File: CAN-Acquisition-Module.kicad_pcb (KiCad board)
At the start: 2 copper layers, 92 x 71 mm, 201 parts, among them J1 Conn_01x04, J10 OSTVN04A150, J11 OSTVN04A150, J12 OSTVN04A150, J13 OSTVN04A150, J2 Conn_01x02, J3 Conn_01x03, J4 Conn_02x05_Odd_Even, J5 OSTVN04A150, J6 OSTVN04A150, J7 USB_B_Micro, J8 OSTVN04A150, J9 OSTVN04A150, Q1 SI2318A, U1 TL431DBZ, U10 BD12734FVJ-E2, U2 S-8581AA, U3 M483SGCAE, U4 SN65HVD234, U5 BD12734FVJ-E2, U6 SCD30, U7 SHT35-DIS, U8 OPA4317IPWR, U9 ERC13232FN-1, Y1 12 MHz

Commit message: Added board settings
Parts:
- moved D2 19.8 mm to (37.8, 26.5)
- moved D6 1.42 mm to (100.4, 63.7), turned to 180 degrees
- moved D1 0.40 mm to (36.7, 23.0)
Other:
- copper layers 2 -> 4
- rule pad_to_mask_clearance: 0 -> 0.05

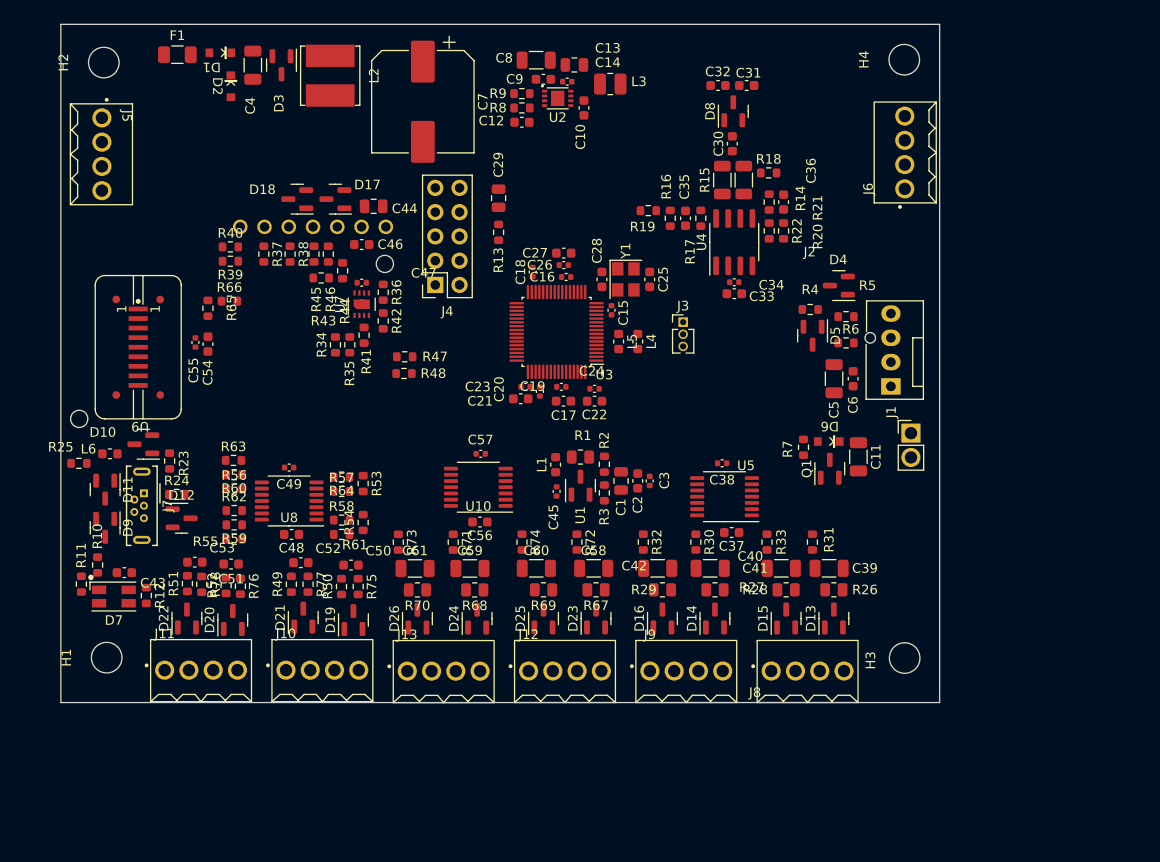
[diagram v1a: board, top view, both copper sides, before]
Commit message: Layout of analog section started
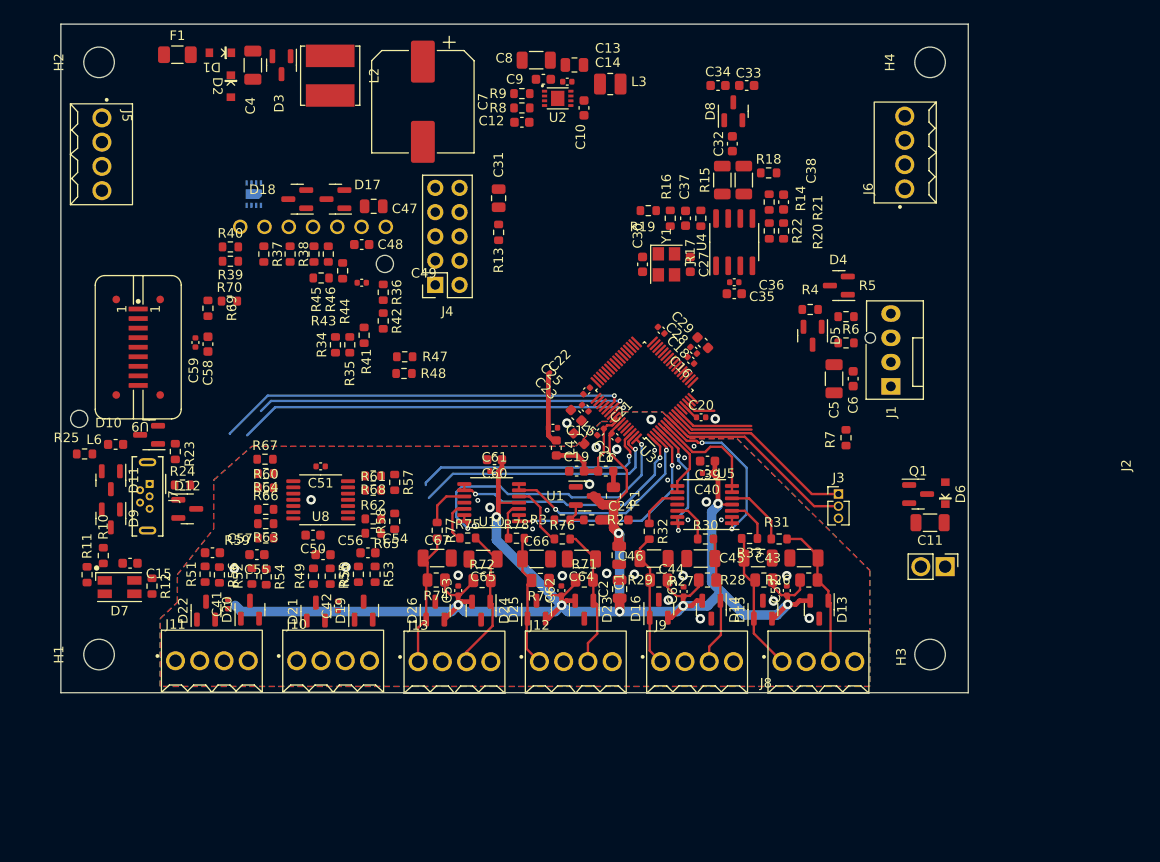
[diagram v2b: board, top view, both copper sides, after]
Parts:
- removed C3: 100 nF, Capacitor_SMD:C_0402_1005Metric
- added C41: 100 nF, Capacitor_SMD:C_0402_1005Metric, F.Cu at (37.5, 80.7)
- added C42: 100 nF, Capacitor_SMD:C_0402_1005Metric, F.Cu at (49.0, 80.9)
- added C52: 100 nF, Capacitor_SMD:C_0402_1005Metric, F.Cu at (96.0, 79.3)
- added C53: 100 nF, Capacitor_SMD:C_0402_1005Metric, F.Cu at (61.6, 79.3)
- added C62: 100 nF, Capacitor_SMD:C_0402_1005Metric, F.Cu at (72.4, 79.3)
- added C63: 100 nF, Capacitor_SMD:C_0402_1005Metric, F.Cu at (85.2, 79.4)
- C2: value 1 uF -> 10 uF; footprint Capacitor_SMD:C_0603_1608Metric -> Capacitor_SMD:C_0805_2012Metric
- U7: moved to B.Cu
- moved J3 24.3 mm to (101.4, 69.2)
- moved C20 23.3 mm to (87.0, 61.2), turned to 0 degrees
- moved C29 17.3 mm to (87.2, 53.4), turned to -45 degrees
- moved C28 16.3 mm to (86.2, 54.1), turned to -45 degrees
- moved U7 16.1 mm to (40.2, 37.8)
- moved J2 14.4 mm to (112.6, 76.8), turned to -90 degrees
- moved L4 14.0 mm to (71.9, 64.4)
- moved D6 13.3 mm to (112.6, 69.1), turned to 90 degrees
- moved C24 12.7 mm to (78.6, 71.9), turned to 0 degrees
- moved C2 11.5 mm to (78.5, 79.2), turned to 90 degrees
- moved C18 11.4 mm to (82.8, 52.0), turned to 135 degrees
- moved U3 11.1 mm to (81.1, 58.4), turned to 135 degrees
- moved L5 11.0 mm to (74.2, 63.4), turned to -45 degrees
- moved C11 10.2 mm to (111.0, 72.2), turned to 180 degrees
- moved C16 9.82 mm to (86.0, 55.2), turned to -45 degrees
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- renumbered C43 to C15, C15 to C16, C45 to C17, C16 to C18, C17 to C19, C18 to C20, C19 to C21, C20 to C22, C21 to C23, C22 to C24, C23 to C25, C24 to C26, C25 to C27, C26 to C28, C27 to C29, C28 to C30, C29 to C31, C30 to C32, C31 to C33, C32 to C34, C33 to C35, C34 to C36, C35 to C37, C36 to C38, C37 to C39, C38 to C40, C39 to C43, C40 to C44, C41 to C45, C42 to C46, C44 to C47, C46 to C48, C47 to C49, C48 to C50, C49 to C51, C50 to C54, C51 to C55, C52 to C56, C53 to C57, C54 to C58, C55 to C59, C56 to C60, C57 to C61, C58 to C64, C59 to C65, C60 to C66, C61 to C67, R75 to R53, R76 to R54, R77 to R55, R78 to R56, R53 to R57, R54 to R58, R55 to R59, R56 to R60, R57 to R61, R58 to R62, R59 to R63, R60 to R64, R61 to R65, R62 to R66, R63 to R67, R64 to R68, R65 to R69, R66 to R70, R67 to R71, R68 to R72, R69 to R73, R70 to R74, R71 to R75, R72 to R76, R73 to R77, R74 to R78
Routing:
- net +1V8: track 0.00 -> 168.5 mm, vias 0 -> 8
- net Net-(R10-Pad1): track 0.00 -> 43.7 mm, vias 0 -> 1
- net Net-(R12-Pad1): track 0.00 -> 42.1 mm, vias 0 -> 1
- net Net-(R11-Pad1): track 0.00 -> 39.6 mm, vias 0 -> 1
- net /ADC7: track 0.00 -> 30.9 mm, vias 0 -> 2
- net /ADC6: track 0.00 -> 27.0 mm, vias 0 -> 2
- net /ADC8: track 0.00 -> 26.9 mm, vias 0 -> 1
- net /ADC9: track 0.00 -> 26.0 mm, vias 0 -> 1
- net /ADC4: track 0.00 -> 24.6 mm, vias 0 -> 2
- net /ADC5: track 0.00 -> 22.9 mm, vias 0 -> 2
- net Net-(J3-Pad2): track 0.00 -> 21.2 mm
- net Net-(J3-Pad1): track 0.00 -> 20.5 mm
- net /ADC0: track 0.00 -> 18.5 mm, vias 0 -> 2
- net Net-(C43-Pad1): track 0.00 -> 15.6 mm
- net Net-(C45-Pad1): track 0.00 -> 15.4 mm
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- added copper zone on B.Cu, net GNDA
- added copper zone on F.Cu, net GNDA
- added copper zone on In1.Cu, net GNDA
- added copper zone on In2.Cu, net GNDA
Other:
- board size 92 x 71 mm -> 95 x 70 mm

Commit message: Analog section, screen and USB finished
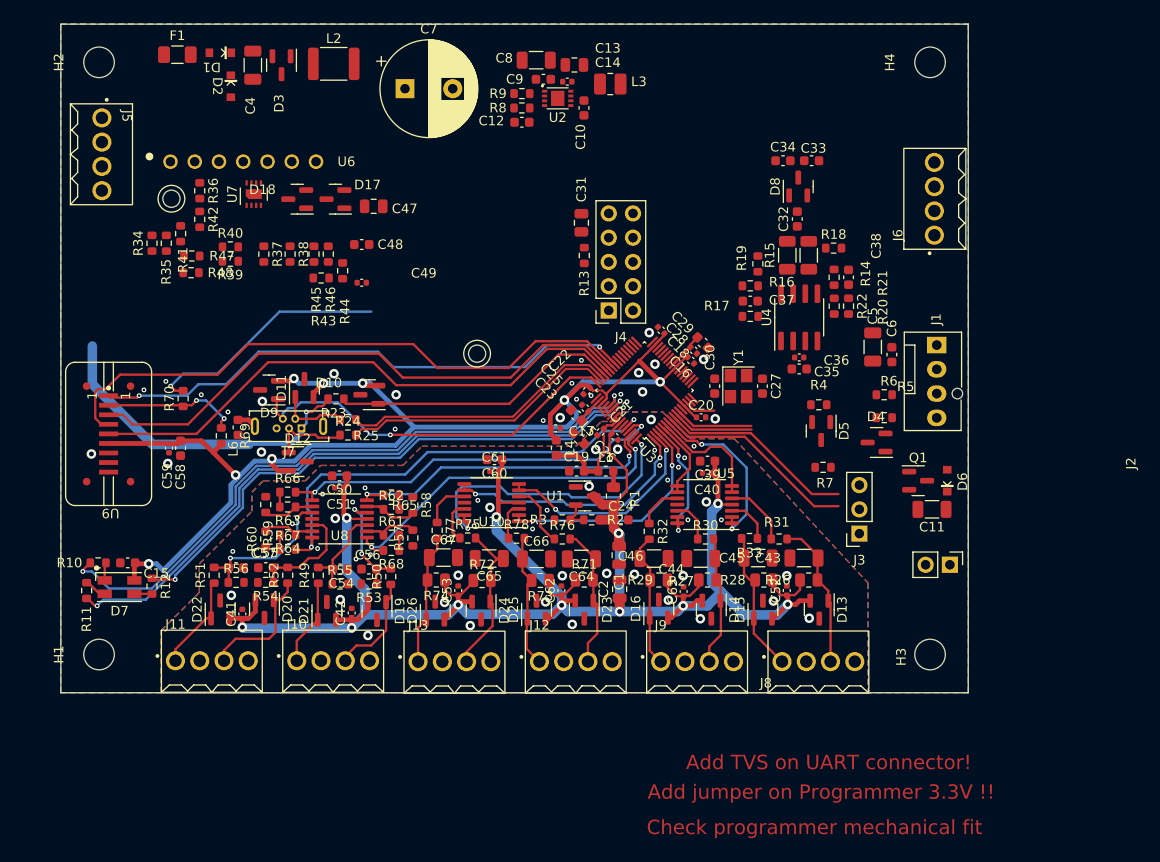
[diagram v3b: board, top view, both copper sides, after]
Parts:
- C7: footprint Capacitor_SMD:CP_Elec_10x10.5 -> Capacitor_THT:CP_Radial_D10.0mm_P5.00mm
- J3: footprint Connector_PinHeader_1.27mm:PinHeader_1x03_P1.27mm_Vertical -> Connector_PinSocket_2.54mm:PinSocket_1x03_P2.54mm_Vertical
- L2: value 330 uF -> 470 uF; footprint Inductor_SMD:L_Bourns_SRN6045TA -> CAN-Acquisition-Module:Murata_LQH43_1812(4532_Metric)
- U6, U7: moved to F.Cu
- moved R25 27.8 mm to (50.1, 61.4), turned to 0 degrees
- moved R47 24.7 mm to (33.7, 44.3)
- moved R48 24.7 mm to (33.6, 46.0)
- moved U6 23.6 mm to (31.5, 34.4), turned to 0 degrees
- moved D10 23.4 mm to (52.3, 58.8)
- moved D11 22.4 mm to (45.5, 58.1), turned to 90 degrees
- moved R34 22.0 mm to (29.5, 42.9)
- moved R35 22.0 mm to (31.0, 42.9)
- moved R36 22.0 mm to (34.5, 37.4)
- moved R41 22.0 mm to (32.5, 41.9)
- moved R42 22.0 mm to (34.5, 40.4)
- moved D9 21.3 mm to (41.8, 58.3), turned to 180 degrees
- moved J4 18.4 mm to (77.4, 50.0)
- moved R24 18.1 mm to (50.0, 63.0)
- moved R23 17.7 mm to (48.8, 59.2), turned to 0 degrees
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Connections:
- C56 pad 1: Net-(C56-Pad1) -> Net-(U8-Pad3)
- J4 pad 1: unconnected-(J4-Pad1) -> +3V3
- J4 pad 10: GND -> /MCU/UART0_RX
- J4 pad 2: +3V3 -> unconnected-(J4-Pad2)
- J4 pad 3: unconnected-(J4-Pad3) -> /MCU/ICE_DAT
- J4 pad 4: /MCU/ICE_DAT -> unconnected-(J4-Pad4)
- J4 pad 5: unconnected-(J4-Pad5) -> /MCU/ICE_CLK
- J4 pad 6: /MCU/ICE_CLK -> unconnected-(J4-Pad6)
- J4 pad 7: /MCU/UART0_TX -> /MCU/nRESET
- J4 pad 8: /MCU/nRESET -> /MCU/UART0_TX
- J4 pad 9: /MCU/UART0_RX -> GND
- R49 pad 2: Net-(C56-Pad1) -> Net-(U8-Pad3)
- R55 pad 1: Net-(C56-Pad1) -> Net-(U8-Pad3)
- U3 pad 8: Net-(J3-Pad2) -> Net-(J3-Pad1)
- U3 pad 9: Net-(J3-Pad1) -> Net-(J3-Pad2)
- U8 pad 1: /ADC9 -> /ADC8
- U8 pad 10: Net-(C55-Pad1) -> Net-(C57-Pad1)
- U8 pad 12: Net-(C57-Pad1) -> Net-(C55-Pad1)
- U8 pad 13: Net-(R59-Pad2) -> Net-(R60-Pad2)
- U8 pad 14: /ADC10 -> /ADC11
- U8 pad 2: Net-(R58-Pad2) -> Net-(R57-Pad2)
- U8 pad 3: Net-(C54-Pad1) -> Net-(U8-Pad3)
- U8 pad 5: Net-(C56-Pad1) -> Net-(C54-Pad1)
- U8 pad 6: Net-(R57-Pad2) -> Net-(R58-Pad2)
- U8 pad 7: /ADC8 -> /ADC9
- U8 pad 8: /ADC11 -> /ADC10
- U8 pad 9: Net-(R60-Pad2) -> Net-(R59-Pad2)
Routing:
- net +3V3: track 9.42 -> 141.2 mm, vias 0 -> 8
- net /MCU/SCREEN_CLK: track 0.00 -> 63.9 mm
- net /MCU/SCREEN_COMMAND/DATA: track 0.00 -> 59.4 mm
- net /MCU/SCREEN_MOSI: track 0.00 -> 58.8 mm
- net /MCU/SCREEN_SS: track 0.00 -> 57.6 mm, vias 0 -> 2
- net /ADC11: track 0.00 -> 47.8 mm, vias 0 -> 2
- net /ADC10: track 0.00 -> 42.4 mm, vias 0 -> 2
- net /MCU/USB_OTG_ID: track 0.00 -> 40.2 mm, vias 0 -> 1
- net /Power/V_USB: track 0.00 -> 34.3 mm, vias 0 -> 1
- net /MCU/USB_VBUS: track 0.00 -> 30.6 mm
- net /MCU/USB_D-: track 0.00 -> 29.1 mm
- net /MCU/USB_D+: track 0.00 -> 28.8 mm
- net +1V8: track 168.5 -> 197.0 mm, vias 8 -> 11
- net Net-(R11-Pad1): track 39.6 -> 67.8 mm, vias 1 -> 2
- net /MCU/PERIPHERAL_RESET: track 0.00 -> 25.7 mm, vias 0 -> 1
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- added copper zone on B.Cu, net GND
- added copper zone on F.Cu, net GND
- added copper zone on In1.Cu, net GND
- added copper zone on In2.Cu, net GND
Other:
- board text added: "Add TVS on UART connector!"
- board text added: "Add jumper on Programmer 3.3V !!"
- board text added: "Check programmer mechanical fit"

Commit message: Finished power outputs
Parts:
- added D8: CM1213A-01SO, Package_TO_SOT_SMD:SOT-23, F.Cu at (102.9, 78.7)
- added D9: CM1213A-01SO, Package_TO_SOT_SMD:SOT-23, F.Cu at (98.4, 67.1)
- added R13: Ω, Resistor_SMD:R_0603_1608Metric, F.Cu at (74.8, 49.3)
- J4: footprint Connector_PinSocket_2.54mm:PinSocket_2x05_P2.54mm_Vertical -> CAN-Acquisition-Module:Nu-Link-Me-v3.0
- L2: value 470 uF -> 470 uH
- R48: renamed from R47; value 1.1 kΩ -> 1 kΩ
- R49: renamed from R48; value 1.1 kΩ -> 1 kΩ
- U1: value TL431DBZ -> AZ431LAN
- moved D6 19.6 mm to (112.4, 48.2), turned to 180 degrees
- moved C11 19.5 mm to (87.8, 30.2)
- moved C12 19.5 mm to (93.2, 24.2)
- moved C13 19.5 mm to (92.5, 25.9)
- moved C7 19.5 mm to (89.2, 23.7)
- moved C8 19.5 mm to (90.0, 25.7)
- moved C9 19.5 mm to (94.2, 28.7)
- moved L3 19.5 mm to (97.0, 26.2)
- moved R8 19.5 mm to (87.8, 28.7)
- moved R9 19.5 mm to (87.8, 27.2)
- moved U2 19.5 mm to (91.5, 27.7)
- moved R5 18.2 mm to (106.6, 79.4), turned to -90 degrees
- moved C10 17.1 mm to (111.9, 53.7)
- moved Q1 17.1 mm to (110.5, 50.7)
- moved J2 16.7 mm to (112.3, 59.9)
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- renumbered C11 to C10, C12 to C11, C13 to C12, C14 to C13, C15 to C14, C16 to C15, C17 to C16, C18 to C17, C19 to C18, C20 to C19, C21 to C20, C22 to C21, C23 to C22, C24 to C23, C25 to C24, C26 to C25, C27 to C26, C28 to C27, C29 to C28, C30 to C29, C4 to C3, C31 to C30, C32 to C31, C33 to C32, C34 to C33, C35 to C34, C36 to C35, C37 to C36, C38 to C37, C39 to C38, C40 to C39, C5 to C4, C41 to C40, C42 to C41, C43 to C42, C44 to C43, C45 to C44, C46 to C45, C47 to C46, C48 to C47, C49 to C48, C50 to C49, C6 to C5, C51 to C50, C52 to C51, C53 to C52, C54 to C53, C55 to C54, C56 to C55, C57 to C56, C58 to C57, C59 to C58, C60 to C59, C7 to C6, C61 to C60, C62 to C61, C63 to C62, C64 to C63, C65 to C64, C66 to C65, C67 to C66, C8 to C7, C9 to C8, C10 to C9, D8 to D10, D9 to D11, D10 to D12, D11 to D13, D12 to D14, D13 to D15, D14 to D16, D15 to D17, D16 to D18, D17 to D19, D18 to D20, D19 to D21, D20 to D22, D21 to D23, D22 to D24, D23 to D25, D24 to D26, D25 to D27, D26 to D28, R13 to R14, R14 to R15, R15 to R16, R16 to R17, R17 to R18, R18 to R19, R19 to R20, R20 to R21, R21 to R22, R22 to R23, R23 to R24, R24 to R25, R25 to R26, R26 to R27, R27 to R28, R28 to R29, R29 to R30, R30 to R31, R31 to R32, R32 to R33, R33 to R34, R34 to R35, R35 to R36, R36 to R37, R37 to R38, R38 to R39, R39 to R40, R40 to R41, R41 to R42, R42 to R43, R43 to R44, R44 to R45, R45 to R46, R46 to R47, R49 to R50, R50 to R51, R51 to R52, R52 to R53, R53 to R54, R54 to R55, R55 to R56, R56 to R57, R57 to R58, R58 to R59, R59 to R60, R60 to R61, R61 to R62, R62 to R63, R63 to R64, R64 to R65, R65 to R66, R66 to R67, R67 to R68, R68 to R69, R69 to R70, R70 to R71, R71 to R72, R72 to R73, R73 to R74, R74 to R75, R75 to R76, R76 to R77, R77 to R78, R78 to R79
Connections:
- J4 pad 1: +3V3 -> GND
- J4 pad 10: /MCU/UART0_RX -> unconnected-(J4-Pad10)
- J4 pad 2: unconnected-(J4-Pad2) -> /MCU/UART0_RX
- J4 pad 3: /MCU/ICE_DAT -> /MCU/nRESET
- J4 pad 4: unconnected-(J4-Pad4) -> /MCU/UART0_TX
- J4 pad 7: /MCU/nRESET -> /MCU/ICE_DAT
- J4 pad 8: /MCU/UART0_TX -> unconnected-(J4-Pad8)
- J4 pad 9: GND -> Net-(J4-Pad9)
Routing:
- net +3V3: track 141.2 -> 189.3 mm, vias 8 -> 12
- net VBUS: track 0.00 -> 31.1 mm
- net /MCU/FAN_PWM_CTRL: track 8.13 -> 39.0 mm, vias 0 -> 2
- net /MCU/FAN_TACH: track 8.48 -> 31.0 mm
- net Net-(Q1-Pad1): track 0.00 -> 20.4 mm
- net Net-(D6-Pad2): track 0.00 -> 12.7 mm
- net Net-(C26-Pad2): track 0.00 -> 9.28 mm
- net /MCU/POWER_OUT: track 3.12 -> 11.5 mm
- net Net-(J1-Pad4): track 0.00 -> 6.62 mm
- net Net-(D8-Pad1): track 21.2 -> 27.1 mm
- net Net-(C29-Pad1): track 0.00 -> 5.76 mm
- net Net-(J1-Pad3): track 0.00 -> 5.05 mm
- net Net-(D9-Pad1): track 20.5 -> 22.6 mm
- net /ADC0: track 18.5 -> 16.6 mm
- net +1V8: track 197.0 -> 198.2 mm
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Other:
- board text added: "Check programmer mechanical fit!"
- board text removed: "Add TVS on UART connector!"
- board text removed: "Add jumper on Programmer 3.3V !!"
- board text removed: "Check programmer mechanical fit"

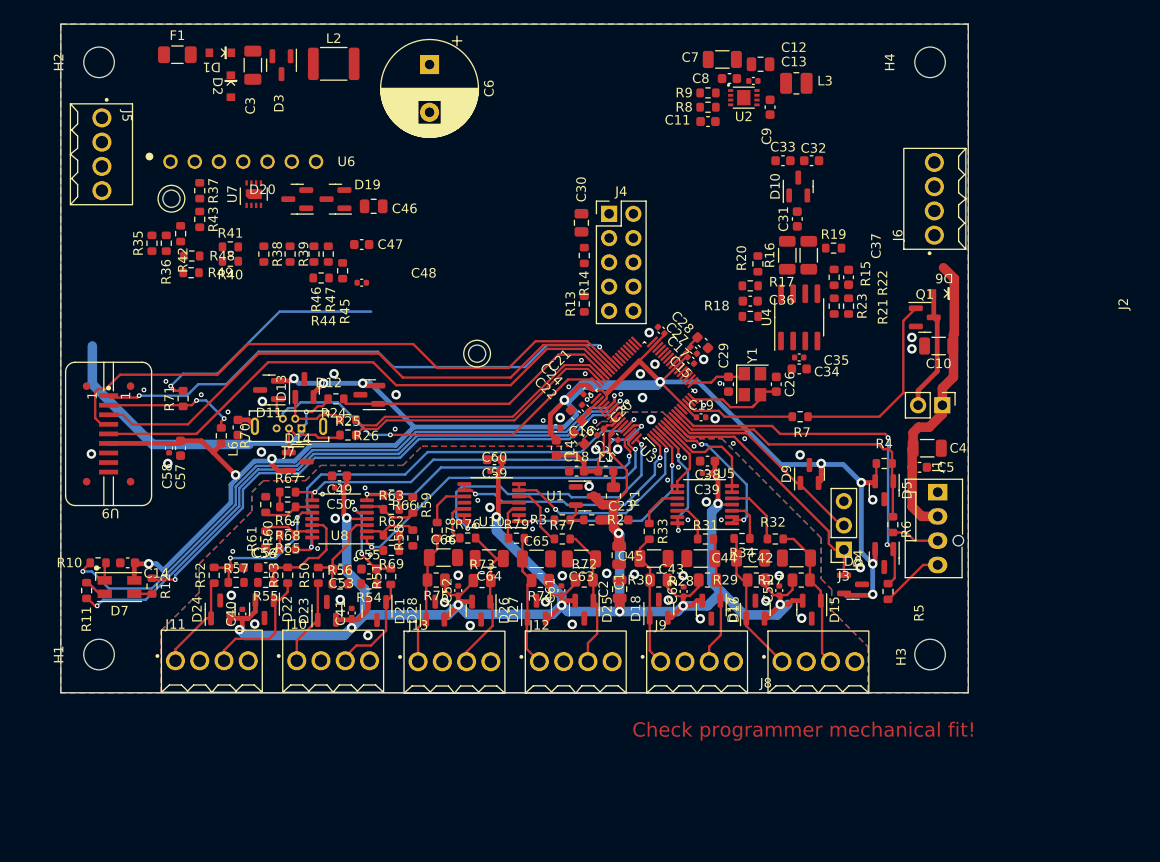
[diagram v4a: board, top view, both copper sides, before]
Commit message: Only CAN transceiver left
SPi flash should be added too
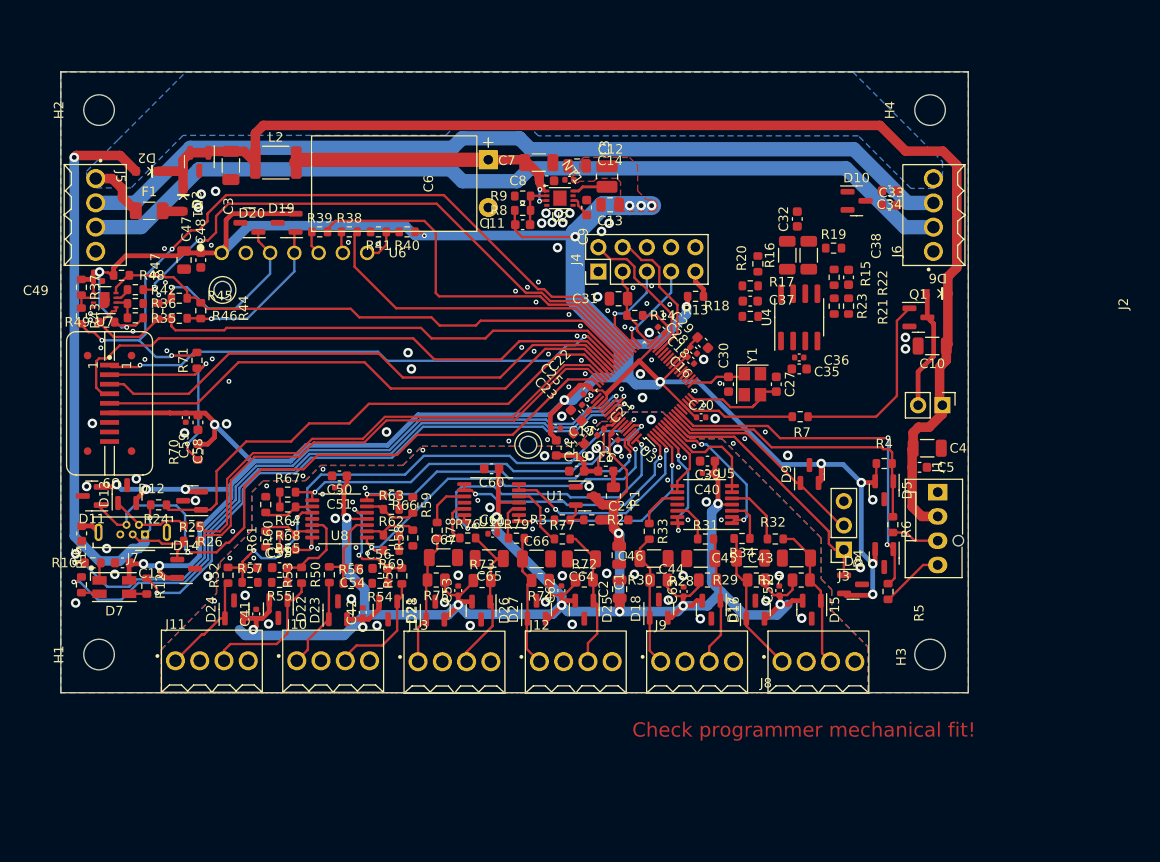
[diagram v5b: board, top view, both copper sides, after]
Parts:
- added C13: 10 uF, Capacitor_SMD:C_0805_2012Metric, F.Cu at (77.5, 38.9)
- added NT1: NetTie_2, CAN-Acquisition-Module:Net_Tie_small, F.Cu at (73.1, 35.8)
- C6: footprint Capacitor_THT:CP_Radial_D10.0mm_P5.00mm -> CAN-Acquisition-Module:CP_Radial_D10.0mm_P5.00mm_Horizontal
- moved C49 27.6 mm to (23.9, 46.9), turned to 0 degrees
- moved C11 22.2 mm to (68.3, 41.0)
- moved R8 22.2 mm to (68.3, 39.5)
- moved R9 22.2 mm to (68.3, 38.0)
- moved L3 22.1 mm to (77.2, 36.0), turned to 90 degrees
- moved C7 22.0 mm to (70.0, 34.5)
- moved C12 22.0 mm to (74.0, 34.9)
- moved U2 21.9 mm to (72.2, 38.2)
- moved C8 21.9 mm to (70.9, 36.4)
- moved C9 21.9 mm to (75.0, 39.2)
- moved C14 21.9 mm to (73.2, 36.3)
- moved D12 21.6 mm to (33.7, 69.9)
- moved D11 21.6 mm to (23.2, 69.4)
- moved D13 21.6 mm to (26.9, 69.2)
- moved R24 21.6 mm to (30.2, 70.3)
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- renumbered C13 to C14, C14 to C15, C15 to C16, C16 to C17, C17 to C18, C18 to C19, C19 to C20, C20 to C21, C21 to C22, C22 to C23, C23 to C24, C24 to C25, C25 to C26, C26 to C27, C27 to C28, C28 to C29, C29 to C30, C30 to C31, C31 to C32, C32 to C33, C33 to C34, C34 to C35, C35 to C36, C36 to C37, C37 to C38, C38 to C39, C39 to C40, C40 to C41, C41 to C42, C42 to C43, C43 to C44, C44 to C45, C45 to C46, C46 to C47, C47 to C48, C48 to C49, C49 to C50, C50 to C51, C51 to C52, C52 to C53, C53 to C54, C54 to C55, C55 to C56, C56 to C57, C57 to C58, C58 to C59, C59 to C60, C60 to C61, C61 to C62, C62 to C63, C63 to C64, C64 to C65, C65 to C66, C66 to C67
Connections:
- D19 pad 2: unconnected-(D19-Pad2) -> +3V3
- D19 pad 3: unconnected-(D19-Pad3) -> GND
- D20 pad 2: unconnected-(D20-Pad2) -> +3V3
- D20 pad 3: unconnected-(D20-Pad3) -> GND
- U2 pad 1: Net-(C6-Pad1) -> Net-(NT1-Pad2)
- U2 pad 3: Net-(C6-Pad1) -> Net-(NT1-Pad2)
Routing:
- net +3V3: track 189.3 -> 326.4 mm, vias 12 -> 20
- net VBUS: track 31.1 -> 134.5 mm
- net /CANbus/CAN_L/GRN: track 0.00 -> 93.8 mm
- net /CANbus/CAN_H/YEL: track 0.00 -> 93.3 mm
- net /MCU/HUMIDITY_ALERT: track 0.00 -> 62.2 mm, vias 0 -> 2
- net /MCU/I2C_SDA: track 0.00 -> 61.6 mm
- net /MCU/I2C_SCL: track 0.00 -> 58.3 mm
- net /MCU/PERIPHERAL_RESET: track 25.7 -> 82.3 mm, vias 1 -> 3
- net /MCU/CO2_RDY: track 0.00 -> 41.3 mm
- net /MCU/CO2_PWM: track 0.00 -> 35.7 mm
- net /MCU/USB_OTG_ID: track 40.1 -> 68.8 mm
- net Net-(C6-Pad1): track 0.00 -> 26.7 mm
- net /Power/V_USB: track 34.3 -> 60.4 mm, vias 1 -> 2
- net /MCU/USB_VBUS: track 30.6 -> 55.8 mm
- net /MCU/USB_D+: track 28.8 -> 52.5 mm
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- added copper zone on F.Cu, net +3V3
- added copper zone on B.Cu, net /CANbus/V+/RED
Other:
- board size 95 x 70 mm -> 95 x 65 mm
